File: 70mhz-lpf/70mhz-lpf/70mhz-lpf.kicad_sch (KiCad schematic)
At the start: 15 parts, among them J701 Coax Solder Point, J702 Coax Solder Point

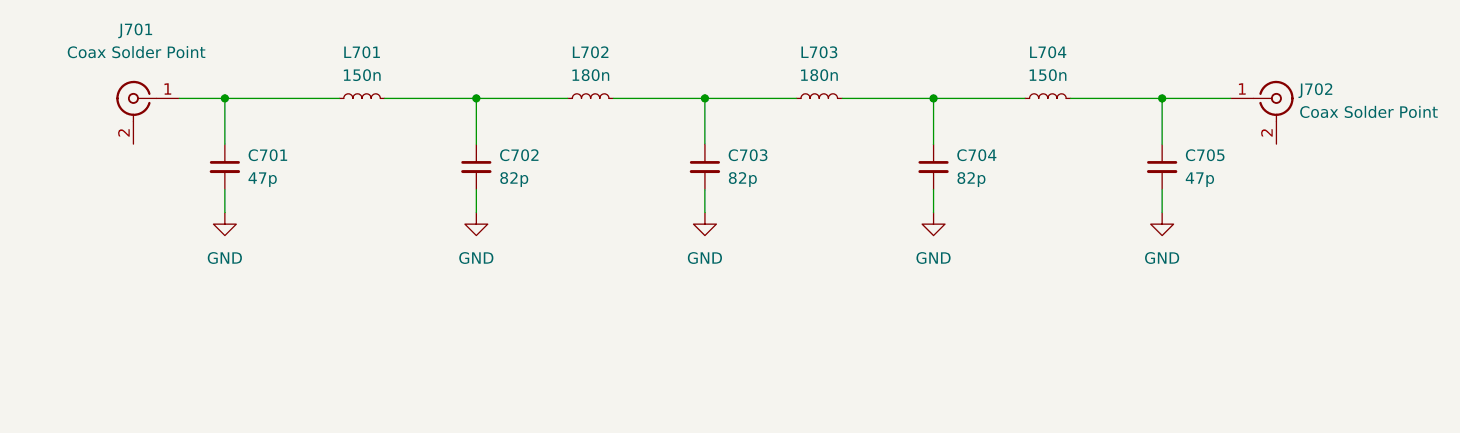
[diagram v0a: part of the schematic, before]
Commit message: Hierarchical schematic updates
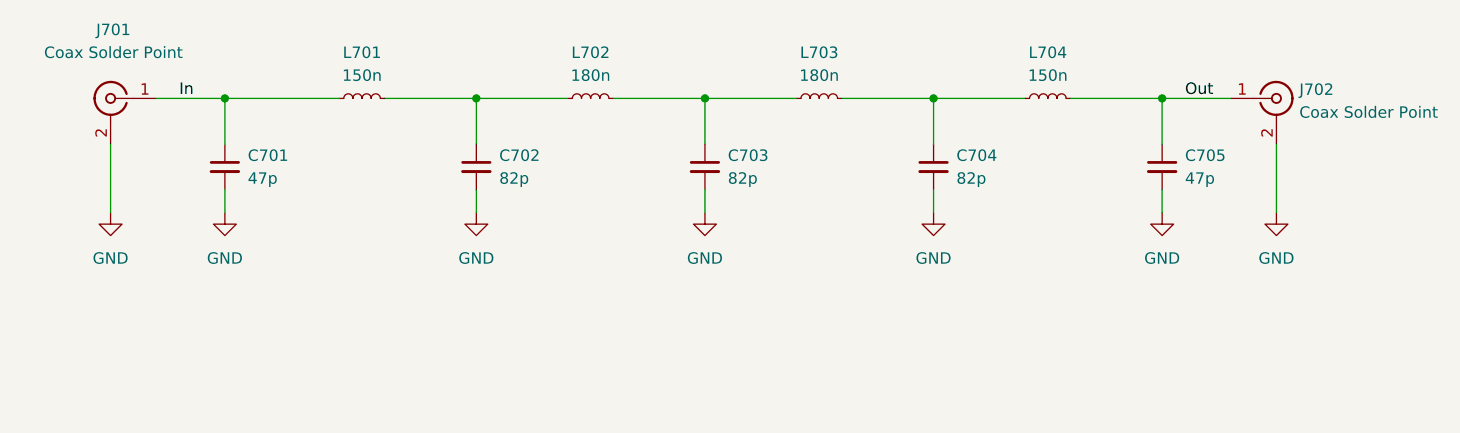
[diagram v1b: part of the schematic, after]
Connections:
- net GND: now also J701.2 (Ext), J702.2 (Ext)
- net Out: now reaches C705.1, J702.1 (In), L704.2
- net In: now reaches C701.1, J701.1 (In), L701.1
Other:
- moved on the sheet: J701
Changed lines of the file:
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@@
+    (stroke (width 0) (type default) (color 0 0 0 0))
+  )
+  (wire (pts (xy 73.66 104.14) (xy 73.66 111.76))
     (stroke (width 0) (type default) (color 0 0 0 0))
   )
@@
     (stroke (width 0) (type default) (color 0 0 0 0))
   )
-  (wire (pts (xy 81.28 99.06) (xy 86.36 99.06))
+  (wire (pts (xy 78.74 99.06) (xy 86.36 99.06))
     (stroke (width 0) (type default) (color 0 0 0 0))
   )
@@
     (stroke (width 0) (type default) (color 0 0 0 0))
   )
+  (wire (pts (xy 203.2 104.14) (xy 203.2 111.76))
+    (stroke (width 0) (type default) (color 0 0 0 0))
+  )
+  (label "In" (at 81.28 99.06 0)
+    (effects (font (size 1.27 1.27)) (justify left bottom))
+  )
+  (label "Out" (at 193.04 99.06 0)
+    (effects (font (size 1.27 1.27)) (justify left bottom))
+  )
   (symbol (lib_id "power:GND") (at 86.36 111.76 0) (unit 1)
     (in_bom yes) (on_board yes) (fields_autoplaced)
-    (property "Reference" "#PWR0701" (id 0) (at 86.36 118.11 0)
+    (property "Reference" "#PWR0702" (id 0) (at 86.36 118.11 0)
       (effects (font (size 1.27 1.27)) hide)
     )
@@
     (pin "2")
   )
+  (symbol (lib_id "power:GND") (at 73.66 111.76 0) (unit 1)
+    (in_bom yes) (on_board yes) (fields_autoplaced)
+    (property "Reference" "#PWR0701" (id 0) (at 73.66 118.11 0)
+      (effects (font (size 1.27 1.27)) hide)
+    )
+    (property "Value" "GND" (id 1) (at 73.66 116.84 0))
+    (property "Footprint" "" (id 2) (at 73.66 111.76 0)
+      (effects (font (size 1.27 1.27)) hide)
+    )
+    (property "Datasheet" "" (id 3) (at 73.66 111.76 0)
+      (effects (font (size 1.27 1.27)) hide)
+    )
+    (pin "1")
+  )
   (symbol (lib_id "Device:C_Small") (at 86.36 106.68 0) (unit 1)
     (in_bom yes) (on_board yes) (fields_autoplaced)
@@
   (symbol (lib_id "power:GND") (at 114.3 111.76 0) (unit 1)
     (in_bom yes) (on_board yes) (fields_autoplaced)
-    (property "Reference" "#PWR0702" (id 0) (at 114.3 118.11 0)
+    (property "Reference" "#PWR0703" (id 0) (at 114.3 118.11 0)
       (effects (font (size 1.27 1.27)) hide)
     )
@@
   (symbol (lib_id "power:GND") (at 139.7 111.76 0) (unit 1)
     (in_bom yes) (on_board yes) (fields_autoplaced)
-    (property "Reference" "#PWR0703" (id 0) (at 139.7 118.11 0)
+    (property "Reference" "#PWR0704" (id 0) (at 139.7 118.11 0)
       (effects (font (size 1.27 1.27)) hide)
     )
@@
   (symbol (lib_id "power:GND") (at 190.5 111.76 0) (unit 1)
     (in_bom yes) (on_board yes) (fields_autoplaced)
-    (property "Reference" "#PWR0705" (id 0) (at 190.5 118.11 0)
+    (property "Reference" "#PWR0706" (id 0) (at 190.5 118.11 0)
       (effects (font (size 1.27 1.27)) hide)
     )
@@
   (symbol (lib_id "power:GND") (at 165.1 111.76 0) (unit 1)
     (in_bom yes) (on_board yes) (fields_autoplaced)
-    (property "Reference" "#PWR0704" (id 0) (at 165.1 118.11 0)
+    (property "Reference" "#PWR0705" (id 0) (at 165.1 118.11 0)
       (effects (font (size 1.27 1.27)) hide)
     )
@@
     (pin "2")
   )
-  (symbol (lib_id "Connector:Conn_Coaxial") (at 76.2 99.06 0) (mirror y) (unit 1)
-    (in_bom yes) (on_board yes) (fields_autoplaced)
-    (property "Reference" "J701" (id 0) (at 76.5174 91.44 0))
-    (property "Value" "Coax Solder Point" (id 1) (at 76.5174 93.98 0))
-    (property "Footprint" "Connector_Wire:SolderWire-0.5sqmm_1x02_P4.6mm_D0.9mm_OD2.1mm" (id 2) (at 76.2 99.06 0)
-      (effects (font (size 1.27 1.27)) hide)
-    )
-    (property "Datasheet" "" (id 3) (at 76.2 99.06 0)
-      (effects (font (size 1.27 1.27)) hide)
-    )
-    (property "Spice_Primitive" "J" (id 4) (at 76.2 99.06 0)
-      (effects (font (size 1.27 1.27)) hide)
-    )
-    (property "Spice_Model" "Conn_Coaxial" (id 5) (at 76.2 99.06 0)
-      (effects (font (size 1.27 1.27)) hide)
-    )
-    (property "Spice_Netlist_Enabled" "N" (id 6) (at 76.2 99.06 0)
-      (effects (font (size 1.27 1.27)) hide)
-    )
-    (pin "1")
-    (pin "2")
+  (symbol (lib_id "Connector:Conn_Coaxial") (at 73.66 99.06 0) (mirror y) (unit 1)
+    (in_bom yes) (on_board yes) (fields_autoplaced)
+    (property "Reference" "J701" (id 0) (at 73.9774 91.44 0))
+    (property "Value" "Coax Solder Point" (id 1) (at 73.9774 93.98 0))
+    (property "Footprint" "Connector_Wire:SolderWire-0.5sqmm_1x02_P4.6mm_D0.9mm_OD2.1mm" (id 2) (at 73.66 99.06 0)
+      (effects (font (size 1.27 1.27)) hide)
+    )
+    (property "Datasheet" "" (id 3) (at 73.66 99.06 0)
+      (effects (font (size 1.27 1.27)) hide)
+    )
+    (property "Spice_Primitive" "J" (id 4) (at 73.66 99.06 0)
+      (effects (font (size 1.27 1.27)) hide)
+    )
+    (property "Spice_Model" "Conn_Coaxial" (id 5) (at 73.66 99.06 0)
+      (effects (font (size 1.27 1.27)) hide)
+    )
+    (property "Spice_Netlist_Enabled" "N" (id 6) (at 73.66 99.06 0)
+      (effects (font (size 1.27 1.27)) hide)
+    )
+    (pin "1")
+    (pin "2")
+  )
+  (symbol (lib_id "power:GND") (at 203.2 111.76 0) (unit 1)
+    (in_bom yes) (on_board yes) (fields_autoplaced)
+    (property "Reference" "#PWR0707" (id 0) (at 203.2 118.11 0)
+      (effects (font (size 1.27 1.27)) hide)
+    )
+    (property "Value" "GND" (id 1) (at 203.2 116.84 0))
+    (property "Footprint" "" (id 2) (at 203.2 111.76 0)
+      (effects (font (size 1.27 1.27)) hide)
+    )
+    (property "Datasheet" "" (id 3) (at 203.2 111.76 0)
+      (effects (font (size 1.27 1.27)) hide)
+    )
+    (pin "1")
   )
   (sheet_instances
@@
   )
   (symbol_instances
+    (path "/4ad4de81-aa9b-4684-aa79-7a8b40c21b0d"
+      (reference "#PWR0701") (unit 1) (value "GND") (footprint "")
+    )
     (path "/0b2e010e-44c7-4613-8841-7c82710a757b"
-      (reference "#PWR0701") (unit 1) (value "GND") (footprint "")
+      (reference "#PWR0702") (unit 1) (value "GND") (footprint "")
     )
     (path "/5452bac9-20ed-4c62-8e90-d2c3c31f5fd9"
-      (reference "#PWR0702") (unit 1) (value "GND") (footprint "")
+      (reference "#PWR0703") (unit 1) (value "GND") (footprint "")
     )
     (path "/757839e4-a159-42c3-94fb-c1bf33caedb4"
-      (reference "#PWR0703") (unit 1) (value "GND") (footprint "")
+      (reference "#PWR0704") (unit 1) (value "GND") (footprint "")
     )
     (path "/dc54c61e-f2db-4d4c-b7d2-21ed18520f12"
-      (reference "#PWR0704") (unit 1) (value "GND") (footprint "")
+      (reference "#PWR0705") (unit 1) (value "GND") (footprint "")
     )
     (path "/8deebb2c-2817-4cd0-a900-a89b420b5b5d"
-      (reference "#PWR0705") (unit 1) (value "GND") (footprint "")
+      (reference "#PWR0706") (unit 1) (value "GND") (footprint "")
+    )
+    (path "/fba17eb8-6206-4f72-b2ef-b9ec7da05bfc"
+      (reference "#PWR0707") (unit 1) (value "GND") (footprint "")
     )
     (path "/500be616-fd19-4de7-93fc-0938930e10d6"

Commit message: update to 15v schematic and trying new theme
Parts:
- H701, H702, H703, H704, J701, J702: now left out of the parts list
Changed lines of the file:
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@@
   )
   (symbol (lib_id "Mechanical:MountingHole") (at 163.195 162.56 0) (unit 1)
-    (in_bom yes) (on_board yes) (fields_autoplaced)
+    (in_bom no) (on_board yes) (fields_autoplaced)
     (property "Reference" "H701" (id 0) (at 165.735 161.2899 0)
       (effects (font (size 1.27 1.27)) (justify left))
@@
   )
   (symbol (lib_id "Mechanical:MountingHole") (at 198.755 162.56 0) (unit 1)
-    (in_bom yes) (on_board yes) (fields_autoplaced)
+    (in_bom no) (on_board yes) (fields_autoplaced)
     (property "Reference" "H703" (id 0) (at 201.295 161.2899 0)
       (effects (font (size 1.27 1.27)) (justify left))
@@
   )
   (symbol (lib_id "Mechanical:MountingHole") (at 180.975 162.56 0) (unit 1)
-    (in_bom yes) (on_board yes) (fields_autoplaced)
+    (in_bom no) (on_board yes) (fields_autoplaced)
     (property "Reference" "H702" (id 0) (at 183.515 161.2899 0)
       (effects (font (size 1.27 1.27)) (justify left))
@@
   )
   (symbol (lib_id "Connector:Conn_Coaxial") (at 203.2 99.06 0) (unit 1)
-    (in_bom yes) (on_board yes) (fields_autoplaced)
+    (in_bom no) (on_board yes) (fields_autoplaced)
     (property "Reference" "J702" (id 0) (at 205.74 98.0831 0)
       (effects (font (size 1.27 1.27)) (justify left))
@@
   )
   (symbol (lib_id "Mechanical:MountingHole") (at 217.805 162.56 0) (unit 1)
-    (in_bom yes) (on_board yes) (fields_autoplaced)
+    (in_bom no) (on_board yes) (fields_autoplaced)
     (property "Reference" "H704" (id 0) (at 220.345 161.2899 0)
       (effects (font (size 1.27 1.27)) (justify left))
@@
   )
   (symbol (lib_id "Connector:Conn_Coaxial") (at 73.66 99.06 0) (mirror y) (unit 1)
-    (in_bom yes) (on_board yes) (fields_autoplaced)
+    (in_bom no) (on_board yes) (fields_autoplaced)
     (property "Reference" "J701" (id 0) (at 73.9774 91.44 0))
     (property "Value" "Coax Solder Point" (id 1) (at 73.9774 93.98 0))

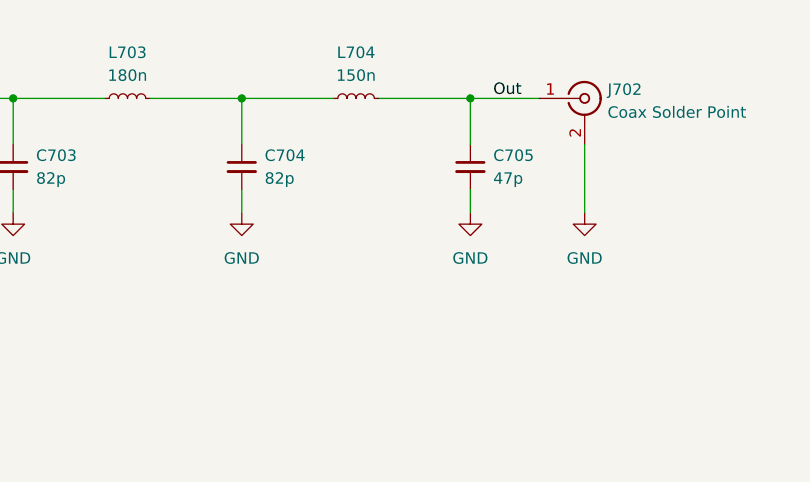
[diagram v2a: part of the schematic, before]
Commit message: minor changes to 5 boards
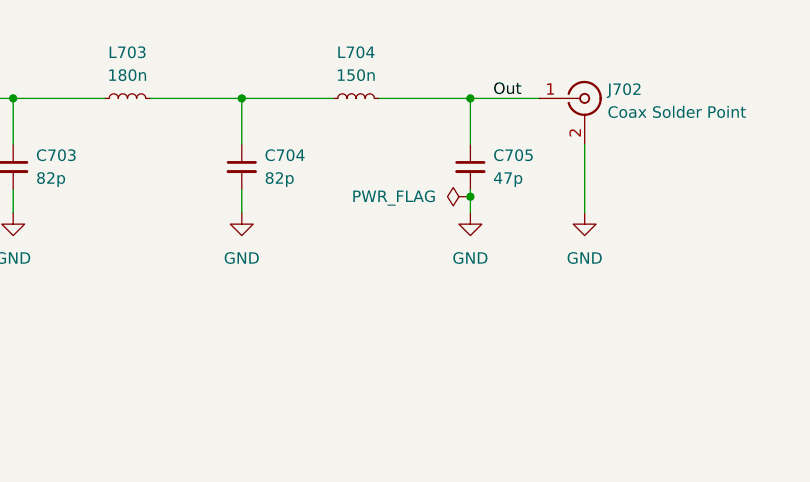
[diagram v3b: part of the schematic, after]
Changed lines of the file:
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@@
   (junction (at 86.36 99.06) (diameter 0) (color 0 0 0 0)
   )
+  (junction (at 190.5 109.982) (diameter 0) (color 0 0 0 0)
+  )
   (junction (at 114.3 99.06) (diameter 0) (color 0 0 0 0)
   )
@@
     (stroke (width 0) (type default) (color 0 0 0 0))
   )
-  (wire (pts (xy 190.5 111.76) (xy 190.5 109.22))
+  (wire (pts (xy 190.5 111.76) (xy 190.5 109.982))
+    (stroke (width 0) (type default) (color 0 0 0 0))
+  )
+  (wire (pts (xy 190.5 109.982) (xy 190.5 109.22))
     (stroke (width 0) (type default) (color 0 0 0 0))
   )
@@
     (pin "1")
   )
+  (symbol (lib_id "power:PWR_FLAG") (at 190.5 109.982 90) (unit 1)
+    (in_bom yes) (on_board yes) (fields_autoplaced)
+    (property "Reference" "#FLG0701" (id 0) (at 188.595 109.982 0)
+      (effects (font (size 1.27 1.27)) hide)
+    )
+    (property "Value" "PWR_FLAG" (id 1) (at 186.69 109.9819 90)
+      (effects (font (size 1.27 1.27)) (justify left))
+    )
+    (property "Footprint" "" (id 2) (at 190.5 109.982 0)
+      (effects (font (size 1.27 1.27)) hide)
+    )
+    (property "Datasheet" "~" (id 3) (at 190.5 109.982 0)
+      (effects (font (size 1.27 1.27)) hide)
+    )
+    (pin "1")
+  )
   (symbol (lib_id "Device:C_Small") (at 86.36 106.68 0) (unit 1)
     (in_bom yes) (on_board yes) (fields_autoplaced)
@@
   )
   (symbol_instances
+    (path "/4cf659fa-3f32-4789-8275-b869e4eaff76"
+      (reference "#FLG0701") (unit 1) (value "PWR_FLAG") (footprint "")
+    )
     (path "/4ad4de81-aa9b-4684-aa79-7a8b40c21b0d"
       (reference "#PWR0701") (unit 1) (value "GND") (footprint "")

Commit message: minor changes for spice
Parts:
- added V701: VSIN, symbol Simulation_SPICE:VSIN
- H701, H702, H703, H704: Spice_Netlist_Enabled (none) -> N; Spice_Primitive (none) -> R
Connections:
- net GND: now also V701.2
- net In: now also V701.1
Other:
- note added: ".ac dec 1001 1E6 500E6"
- note added: "Spice Simulation"

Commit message: 70MHz spice model update
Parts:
- V701: Spice_Model ac 1 -> dc 0 ac 1
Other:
- note added: ".ac dec 1001 1.0k 200.0Meg"
- note removed: ".ac dec 1001 1E6 500E6"
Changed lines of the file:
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@@
     (stroke (width 0) (type default) (color 0 0 0 0))
   )
-  (text "Spice Simulation" (at 48.26 165.1 0)
-    (effects (font (size 1.27 1.27)) (justify left bottom))
-  )
-  (text ".ac dec 1001 1E6 500E6" (at 48.26 167.64 0)
+  (text "Spice Simulation" (at 43.18 158.75 0)
+    (effects (font (size 1.27 1.27)) (justify left bottom))
+  )
+  (text ".ac dec 1001 1.0k 200.0Meg" (at 45.72 167.64 0)
     (effects (font (size 1.27 1.27)) (justify left bottom))
   )
@@
       (effects (font (size 1.27 1.27)) (justify left) hide)
     )
-    (property "Spice_Model" "ac 1" (id 6) (at 38.1 175.0701 0)
-      (effects (font (size 1.27 1.27)) (justify left))
-    )
+    (property "Spice_Model" "dc 0 ac 1" (id 6) (at 38.1 175.0701 0)
+      (effects (font (size 1.27 1.27)) (justify left))
+    )

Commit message: v7 conversion
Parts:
- H701, H702, H703, H704: value MountingHole -> ${SIM.PARAMS}; Spice_Netlist_Enabled N -> (none); Spice_Primitive R -> (none)
- J701, J702: Spice_Model Conn_Coaxial -> (none); Spice_Netlist_Enabled N -> (none); Spice_Primitive J -> (none)
- V701: Spice_Model dc 0 ac 1 -> (none); Spice_Netlist_Enabled Y -> (none); Spice_Primitive V -> (none)
